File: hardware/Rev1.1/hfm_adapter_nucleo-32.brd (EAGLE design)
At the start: 101.6 x 82.5 mm, 50 parts, among them IC1 NUCLEO-G431KB, IC10 OPA2992D, IC11 OPA2172D, IC2 M24M02, IC3 IP4234CZ6,115, IC4 LPS25HBTR, IC6 SRV05-4MR6T1GTSSOP6, IC7 TLE4252D, IC8 TLE42764DV, IC9 ADR01_02_03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

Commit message: some small changes
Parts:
- moved R12 11.5 mm to (47.6, 73.0), turned to 90 degrees
- moved R9 9.67 mm to (45.1, 73.0)
- moved C11 7.10 mm to (41.9, 73.0)
- moved C7 6.38 mm to (36.8, 71.8)
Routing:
- net N$5: track 13.3 -> 28.5 mm
- net VIN: track 94.1 -> 97.6 mm
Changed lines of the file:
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@@
 <attribute name="SPICEPREFIX" value="C" x="25.4" y="44.45" size="1.778" layer="27" rot="R90" display="off"/>
 </element>
-<element name="C11" library="rcl" library_urn="urn:adsk.eagle:library:334" package="C0805" package3d_urn="urn:adsk.eagle:package:23617/2" value="1uF" x="48.26" y="69.85" smashed="yes" rot="R90">
-<attribute name="NAME" x="47.625" y="67.31" size="0.762" layer="25" font="vector" rot="R270"/>
-<attribute name="SPICEPREFIX" value="C" x="48.26" y="69.85" size="1.778" layer="27" rot="R90" display="off"/>
+<element name="C11" library="rcl" library_urn="urn:adsk.eagle:library:334" package="C0805" package3d_urn="urn:adsk.eagle:package:23617/2" value="1uF" x="41.91" y="73.025" smashed="yes" rot="R90">
+<attribute name="NAME" x="41.275" y="70.485" size="0.762" layer="25" font="vector" rot="R270"/>
+<attribute name="SPICEPREFIX" value="C" x="41.91" y="73.025" size="1.778" layer="27" rot="R90" display="off"/>
 </element>
 <element name="C12" library="rcl" library_urn="urn:adsk.eagle:library:334" package="PANASONIC_D" package3d_urn="urn:adsk.eagle:package:23424/2" value="10µF  50v" x="15.24" y="73.66" smashed="yes" rot="R270">
@@
 <attribute name="SPICEPREFIX" value="C" x="21.59" y="73.66" size="1.778" layer="27" rot="R90" display="off"/>
 </element>
-<element name="C7" library="rcl" library_urn="urn:adsk.eagle:library:334" package="PANASONIC_C" package3d_urn="urn:adsk.eagle:package:23422/2" value="22µF" x="43.18" y="71.12" smashed="yes" rot="R270">
-<attribute name="NAME" x="45.72" y="74.93" size="0.762" layer="25" font="vector" rot="R180"/>
-<attribute name="SPICEPREFIX" value="C" x="43.18" y="71.12" size="1.778" layer="27" rot="R270" display="off"/>
+<element name="C7" library="rcl" library_urn="urn:adsk.eagle:library:334" package="PANASONIC_C" package3d_urn="urn:adsk.eagle:package:23422/2" value="22µF" x="36.83" y="71.755" smashed="yes" rot="R270">
+<attribute name="NAME" x="39.37" y="75.565" size="0.762" layer="25" font="vector" rot="R180"/>
+<attribute name="SPICEPREFIX" value="C" x="36.83" y="71.755" size="1.778" layer="27" rot="R270" display="off"/>
 </element>
 <element name="C8" library="rcl" library_urn="urn:adsk.eagle:library:334" package="C0805" package3d_urn="urn:adsk.eagle:package:23617/2" value="100nF" x="95.25" y="16.51" smashed="yes" rot="R270">
@@
 <attribute name="SPICEPREFIX" value="R" x="54.61" y="40.64" size="1.778" layer="27" rot="R180" display="off"/>
 </element>
-<element name="R12" library="rcl" library_urn="urn:adsk.eagle:library:334" package="R0805" package3d_urn="urn:adsk.eagle:package:23553/2" value="10k 0.5%" x="36.195" y="74.295" smashed="yes" rot="R270">
-<attribute name="NAME" x="36.83" y="76.835" size="0.762" layer="25" font="vector" rot="R90"/>
-<attribute name="SPICEPREFIX" value="R" x="36.195" y="74.295" size="1.778" layer="27" rot="R270" display="off"/>
+<element name="R12" library="rcl" library_urn="urn:adsk.eagle:library:334" package="R0805" package3d_urn="urn:adsk.eagle:package:23553/2" value="10k 0.5%" x="47.625" y="73.025" smashed="yes" rot="R90">
+<attribute name="NAME" x="46.99" y="70.485" size="0.762" layer="25" font="vector" rot="R270"/>
+<attribute name="SPICEPREFIX" value="R" x="47.625" y="73.025" size="1.778" layer="27" rot="R90" display="off"/>
 </element>
 <element name="R13" library="rcl" library_urn="urn:adsk.eagle:library:334" package="R0805" package3d_urn="urn:adsk.eagle:package:23553/2" value="82k 0.5%" x="54.61" y="52.07" smashed="yes">
@@
 <attribute name="SPICEPREFIX" value="R" x="53.34" y="27.94" size="1.778" layer="27" rot="R180" display="off"/>
 </element>
-<element name="R9" library="rcl" library_urn="urn:adsk.eagle:library:334" package="R0805" package3d_urn="urn:adsk.eagle:package:23553/2" value="30k 0.5%" x="36.195" y="69.215" smashed="yes" rot="R270">
-<attribute name="NAME" x="36.195" y="66.675" size="0.762" layer="25" font="vector" rot="R270"/>
-<attribute name="SPICEPREFIX" value="R" x="36.195" y="69.215" size="1.778" layer="27" rot="R270" display="off"/>
+<element name="R9" library="rcl" library_urn="urn:adsk.eagle:library:334" package="R0805" package3d_urn="urn:adsk.eagle:package:23553/2" value="30k 0.5%" x="45.085" y="73.025" smashed="yes" rot="R270">
+<attribute name="NAME" x="45.085" y="70.485" size="0.762" layer="25" font="vector" rot="R270"/>
+<attribute name="SPICEPREFIX" value="R" x="45.085" y="73.025" size="1.778" layer="27" rot="R270" display="off"/>
 </element>
 <element name="X2" library="con-kycon" library_urn="urn:adsk.eagle:library:157" package="KUSBVX-BS1N" package3d_urn="urn:adsk.eagle:package:7681/1" value="KUSBVX-BS1N" x="28.575" y="17.145" smashed="yes" rot="R270">
@@
 <contactref element="R12" pad="2"/>
 <contactref element="IC8" pad="4"/>
-<wire x1="36.195" y1="70.165" x2="36.195" y2="70.485" width="0.1524" layer="1"/>
-<wire x1="36.195" y1="71.755" x2="36.195" y2="73.345" width="0.1524" layer="1"/>
-<wire x1="36.195" y1="70.485" x2="36.195" y2="71.12" width="0.1524" layer="1"/>
-<wire x1="36.195" y1="71.12" x2="36.195" y2="71.755" width="0.1524" layer="1"/>
 <wire x1="30.35" y1="66.32" x2="30.48" y2="66.45" width="0.1524" layer="1"/>
-<wire x1="30.48" y1="66.45" x2="30.48" y2="67.945" width="0.1524" layer="1"/>
-<wire x1="30.48" y1="67.945" x2="31.115" y2="68.58" width="0.1524" layer="1"/>
-<wire x1="31.115" y1="68.58" x2="33.655" y2="68.58" width="0.1524" layer="1"/>
-<wire x1="33.655" y1="68.58" x2="34.29" y2="69.215" width="0.1524" layer="1"/>
-<wire x1="34.29" y1="71.12" x2="34.29" y2="69.215" width="0.1524" layer="1"/>
-<wire x1="36.195" y1="71.755" x2="34.925" y2="71.755" width="0.1524" layer="1"/>
-<wire x1="34.925" y1="71.755" x2="34.29" y2="71.12" width="0.1524" layer="1"/>
+<wire x1="30.35" y1="66.32" x2="30.35" y2="68.45" width="0.1524" layer="1"/>
+<wire x1="30.35" y1="68.45" x2="31.115" y2="69.215" width="0.1524" layer="1"/>
+<wire x1="31.115" y1="69.215" x2="34.29" y2="69.215" width="0.1524" layer="1"/>
+<wire x1="34.29" y1="69.215" x2="34.925" y2="69.85" width="0.1524" layer="1"/>
+<wire x1="34.925" y1="69.85" x2="34.925" y2="71.12" width="0.1524" layer="1"/>
+<wire x1="34.925" y1="71.12" x2="35.56" y2="71.755" width="0.1524" layer="1"/>
+<wire x1="35.56" y1="71.755" x2="39.37" y2="71.755" width="0.1524" layer="1"/>
+<wire x1="39.37" y1="71.755" x2="40.005" y2="72.39" width="0.1524" layer="1"/>
+<wire x1="40.005" y1="72.39" x2="40.005" y2="75.565" width="0.1524" layer="1"/>
+<wire x1="40.005" y1="75.565" x2="40.64" y2="76.2" width="0.1524" layer="1"/>
+<wire x1="45.085" y1="73.975" x2="46.355" y2="73.975" width="0.1524" layer="1"/>
+<wire x1="45.72" y1="76.2" x2="46.355" y2="75.565" width="0.1524" layer="1"/>
+<wire x1="40.64" y1="76.2" x2="45.72" y2="76.2" width="0.1524" layer="1"/>
+<wire x1="46.355" y1="75.565" x2="46.355" y2="74.295" width="0.1524" layer="1"/>
+<wire x1="46.355" y1="74.295" x2="46.355" y2="73.975" width="0.1524" layer="1"/>
+<wire x1="47.625" y1="73.975" x2="46.355" y2="73.975" width="0.1524" layer="1"/>
 </signal>
 <signal name="VREF">
@@
 <wire x1="48.895" y1="22.86" x2="48.26" y2="23.495" width="0.254" layer="1"/>
 <wire x1="48.895" y1="22.86" x2="66.04" y2="22.86" width="0.254" layer="1"/>
-<wire x1="31.928384375" y1="66.04" x2="36.195" y2="66.04" width="0.254" layer="1"/>
-<wire x1="36.195" y1="68.265" x2="36.195" y2="66.04" width="0.254" layer="1"/>
-<wire x1="48.26" y1="68.9" x2="48.26" y2="68.58" width="0.254" layer="1"/>
-<wire x1="48.26" y1="68.58" x2="48.26" y2="59.69" width="0.254" layer="1"/>
 <wire x1="31.648384375" y1="66.32" x2="31.49" y2="66.32" width="0.254" layer="1"/>
-<wire x1="31.648384375" y1="66.32" x2="31.928384375" y2="66.04" width="0.254" layer="1"/>
 <wire x1="48.26" y1="23.495" x2="48.26" y2="35.56" width="0.254" layer="1"/>
 <wire x1="48.26" y1="35.56" x2="48.26" y2="36.83" width="0.254" layer="1"/>
-<wire x1="50.8" y1="35.24" x2="48.58" y2="35.24" width="0.254" layer="1"/>
+<wire x1="50.8" y1="35.24" x2="48.895" y2="35.24" width="0.254" layer="1"/>
+<wire x1="48.895" y1="35.24" x2="48.58" y2="35.24" width="0.254" layer="1"/>
+<wire x1="31.49" y1="66.32" x2="35.84" y2="66.32" width="0.254" layer="1"/>
+<wire x1="35.84" y1="66.32" x2="36.83" y2="67.31" width="0.254" layer="1"/>
+<wire x1="36.83" y1="67.31" x2="36.83" y2="69.705" width="0.254" layer="1"/>
+<wire x1="36.83" y1="69.705" x2="36.975" y2="69.85" width="0.254" layer="1"/>
+<wire x1="36.975" y1="69.85" x2="41.275" y2="69.85" width="0.254" layer="1"/>
+<wire x1="41.275" y1="69.85" x2="41.91" y2="69.85" width="0.254" layer="1"/>
+<wire x1="41.91" y1="69.85" x2="43.815" y2="69.85" width="0.254" layer="1"/>
+<wire x1="43.815" y1="69.85" x2="44.45" y2="69.85" width="0.254" layer="1"/>
+<wire x1="48.26" y1="59.69" x2="48.26" y2="69.215" width="0.254" layer="1"/>
+<wire x1="48.26" y1="69.215" x2="47.625" y2="69.85" width="0.254" layer="1"/>
+<wire x1="47.625" y1="69.85" x2="45.085" y2="69.85" width="0.254" layer="1"/>
+<wire x1="45.085" y1="69.85" x2="43.815" y2="69.85" width="0.254" layer="1"/>
+<wire x1="45.085" y1="72.075" x2="45.085" y2="69.85" width="0.254" layer="1"/>
+<wire x1="41.91" y1="72.075" x2="41.91" y2="69.85" width="0.254" layer="1"/>
 <wire x1="48.58" y1="35.24" x2="48.26" y2="35.56" width="0.254" layer="1"/>
-<wire x1="43.18" y1="69.07" x2="47.77" y2="69.07" width="0.254" layer="1"/>
-<wire x1="47.77" y1="69.07" x2="48.26" y2="68.58" width="0.254" layer="1"/>
-<wire x1="42.545" y1="66.04" x2="43.18" y2="66.675" width="0.254" layer="1"/>
-<wire x1="43.18" y1="66.675" x2="43.18" y2="69.07" width="0.254" layer="1"/>
-<wire x1="36.195" y1="66.04" x2="42.545" y2="66.04" width="0.254" layer="1"/>
 </signal>
 <signal name="N$9">

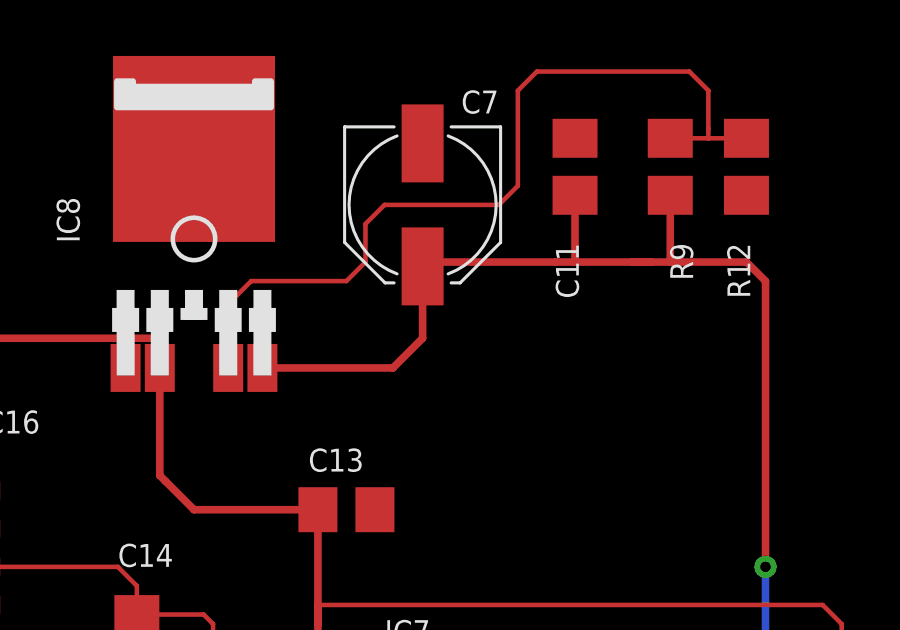
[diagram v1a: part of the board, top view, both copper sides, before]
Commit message: wire stubs removed
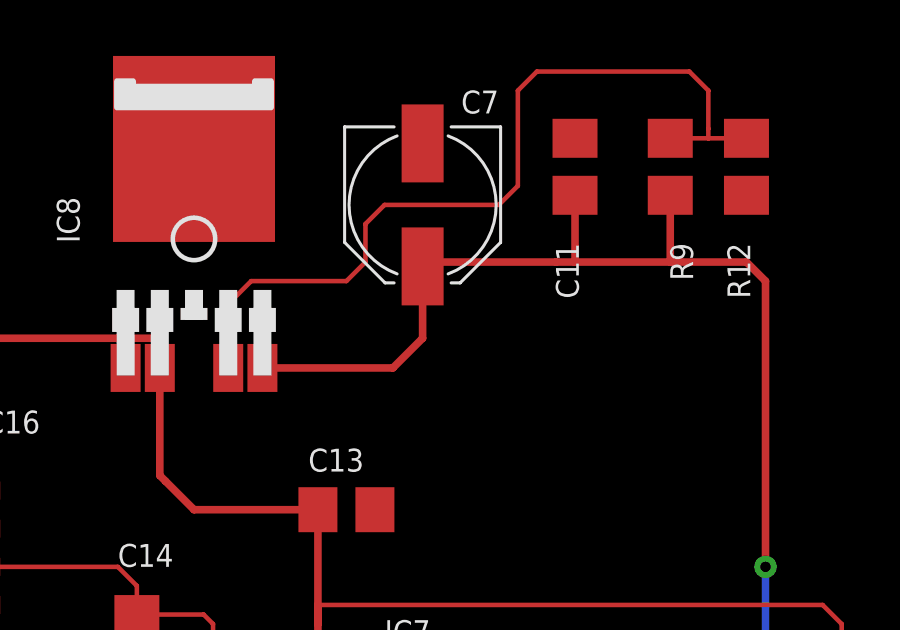
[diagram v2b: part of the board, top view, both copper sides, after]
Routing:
- net VIN: track 97.6 -> 96.8 mm
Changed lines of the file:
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@@
 <contactref element="R12" pad="2"/>
 <contactref element="IC8" pad="4"/>
-<wire x1="30.35" y1="66.32" x2="30.48" y2="66.45" width="0.1524" layer="1"/>
 <wire x1="30.35" y1="66.32" x2="30.35" y2="68.45" width="0.1524" layer="1"/>
 <wire x1="30.35" y1="68.45" x2="31.115" y2="69.215" width="0.1524" layer="1"/>
@@
 <wire x1="48.895" y1="22.86" x2="48.26" y2="23.495" width="0.254" layer="1"/>
 <wire x1="48.895" y1="22.86" x2="66.04" y2="22.86" width="0.254" layer="1"/>
-<wire x1="31.648384375" y1="66.32" x2="31.49" y2="66.32" width="0.254" layer="1"/>
 <wire x1="48.26" y1="23.495" x2="48.26" y2="35.56" width="0.254" layer="1"/>
 <wire x1="48.26" y1="35.56" x2="48.26" y2="36.83" width="0.254" layer="1"/>
 <wire x1="50.8" y1="35.24" x2="48.895" y2="35.24" width="0.254" layer="1"/>
 <wire x1="48.895" y1="35.24" x2="48.58" y2="35.24" width="0.254" layer="1"/>
-<wire x1="31.49" y1="66.32" x2="35.84" y2="66.32" width="0.254" layer="1"/>
-<wire x1="35.84" y1="66.32" x2="36.83" y2="67.31" width="0.254" layer="1"/>
+<wire x1="36.83" y1="67.31" x2="35.84" y2="66.32" width="0.254" layer="1"/>
 <wire x1="36.83" y1="67.31" x2="36.83" y2="69.705" width="0.254" layer="1"/>
 <wire x1="36.83" y1="69.705" x2="36.975" y2="69.85" width="0.254" layer="1"/>
 <wire x1="36.975" y1="69.85" x2="41.275" y2="69.85" width="0.254" layer="1"/>
 <wire x1="41.275" y1="69.85" x2="41.91" y2="69.85" width="0.254" layer="1"/>
-<wire x1="41.91" y1="69.85" x2="43.815" y2="69.85" width="0.254" layer="1"/>
-<wire x1="43.815" y1="69.85" x2="44.45" y2="69.85" width="0.254" layer="1"/>
 <wire x1="48.26" y1="59.69" x2="48.26" y2="69.215" width="0.254" layer="1"/>
 <wire x1="48.26" y1="69.215" x2="47.625" y2="69.85" width="0.254" layer="1"/>
 <wire x1="47.625" y1="69.85" x2="45.085" y2="69.85" width="0.254" layer="1"/>
-<wire x1="45.085" y1="69.85" x2="43.815" y2="69.85" width="0.254" layer="1"/>
 <wire x1="45.085" y1="72.075" x2="45.085" y2="69.85" width="0.254" layer="1"/>
 <wire x1="41.91" y1="72.075" x2="41.91" y2="69.85" width="0.254" layer="1"/>
 <wire x1="48.58" y1="35.24" x2="48.26" y2="35.56" width="0.254" layer="1"/>
+<wire x1="35.84" y1="66.32" x2="31.49" y2="66.32" width="0.254" layer="1"/>
+<wire x1="41.91" y1="69.85" x2="45.085" y2="69.85" width="0.254" layer="1"/>
 </signal>
 <signal name="N$9">
